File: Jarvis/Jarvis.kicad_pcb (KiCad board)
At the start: 2 copper layers, 30 x 50 mm, 137 parts, among them IC1 ADP1607, IC2 MAX-8Q, IC3 MPU-9250, IC4 STM32F411CxUx, IC5 Si4460, IC6 MS5611-01BA03, J1 PYRO, J2 PWR, J3 ARM, P1 SMA, P2 SMA, P3 SWD_TC, Q1 PFET, Q2 PFET, Q3 PFET, Q4 NFET, Q5 NFET, Q6 NFET, Q7 NFET, U1 MICROSD, Y1 26MHz, Y2 30MHz

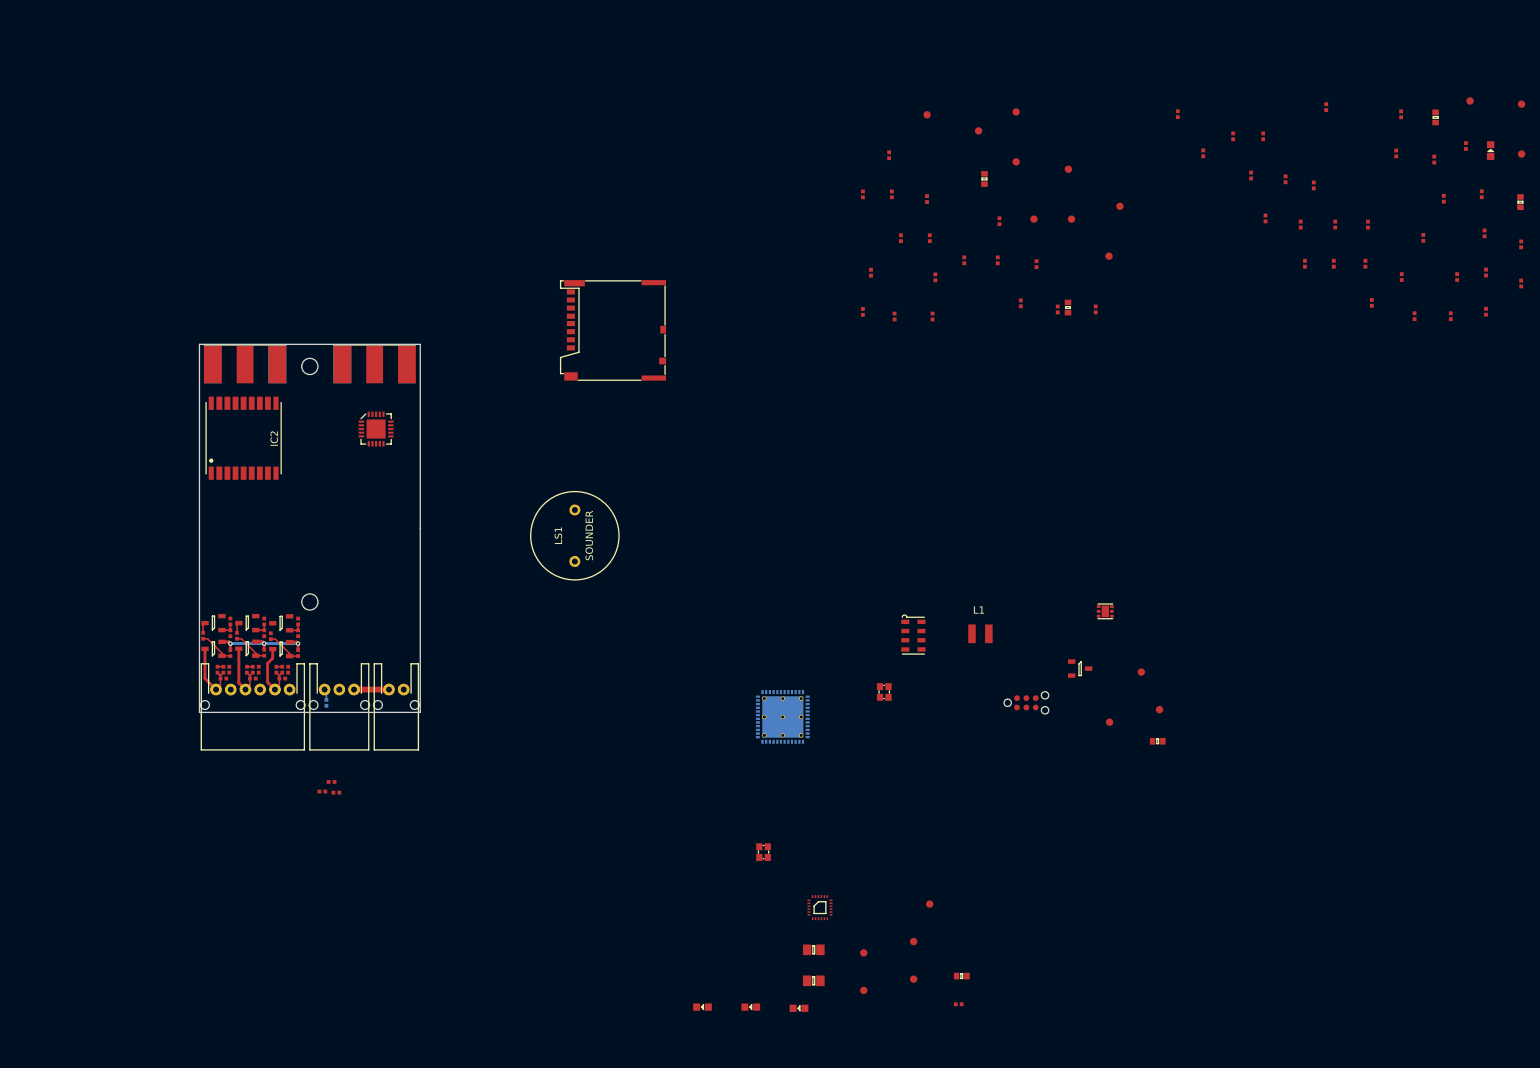
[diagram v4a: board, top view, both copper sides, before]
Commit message: Routed PSU
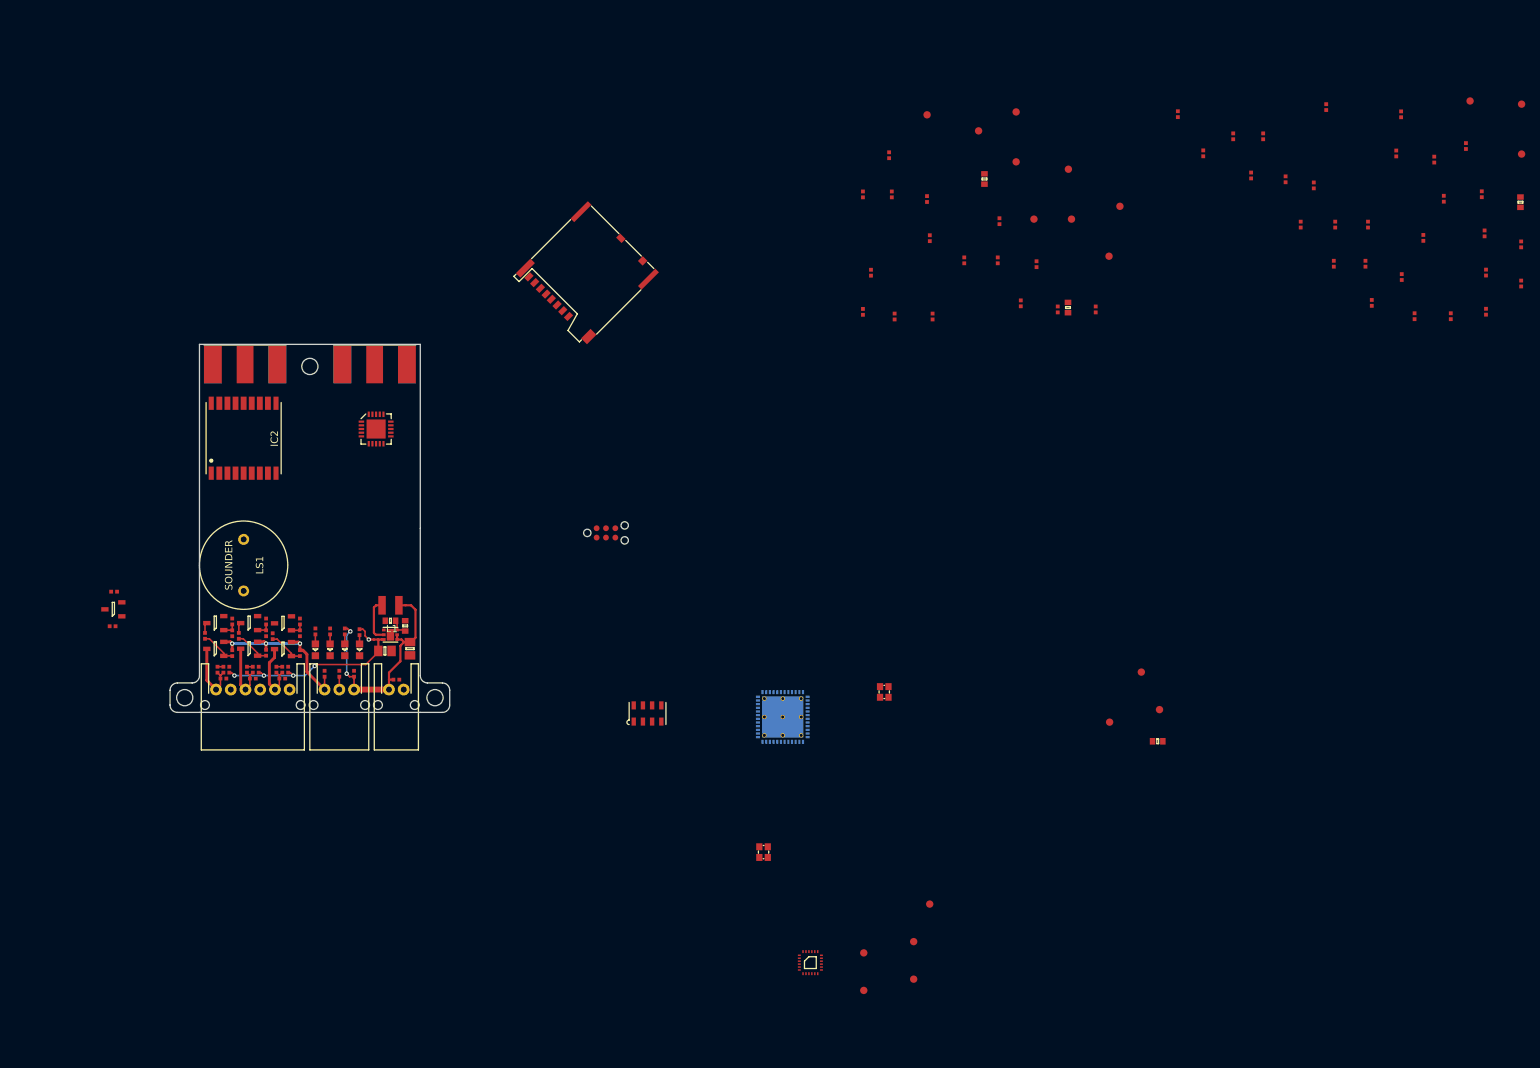
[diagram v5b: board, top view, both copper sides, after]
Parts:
- added REF**: MountingHole_2.2mm_M2_ISO14580, Mounting_Holes:MountingHole_2.2mm_M2_ISO14580, F.Cu at (117.0, 123.0)
- R25: moved to F.Cu
- moved D1 168.0 mm to (106.8, 116.5), turned to 90 degrees
- moved R34 167.8 mm to (73.4, 108.6), turned to 180 degrees
- moved R33 166.1 mm to (73.2, 113.3), turned to 0 degrees
- moved R23 160.5 mm to (102.8, 114.0)
- moved R7 156.1 mm to (113.0, 113.2), turned to 90 degrees
- moved Q7 131.6 mm to (73.3, 111.0), turned to 180 degrees
- moved R24 101.0 mm to (100.8, 114.0), turned to 270 degrees
- moved IC1 97.2 mm to (111.0, 114.5), turned to 180 degrees
- moved R22 92.5 mm to (104.8, 114.0)
- moved R21 91.9 mm to (106.8, 114.1)
- moved R11 91.4 mm to (111.0, 112.5), turned to 180 degrees
- moved L1 80.2 mm to (111.0, 110.5), turned to 180 degrees
- moved D2 78.6 mm to (104.8, 116.5), turned to 90 degrees
- moved D3 75.0 mm to (102.8, 116.5), turned to 90 degrees
- moved C3 73.5 mm to (110.2, 116.7)
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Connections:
- J3 pad 1: Net-(J3-Pad1) -> /PYRO_SO
- J3 pad 2: /PYRO_SO -> Net-(J3-Pad2)
- R25 pad 1: Net-(J3-Pad1) -> Net-(J3-Pad2)
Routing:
- net 3v3: track 0.00 -> 30.0 mm, vias 0 -> 5
- net VBATT: track 4.75 -> 33.1 mm, vias 0 -> 2
- net /PYRO_SO: track 15.8 -> 24.9 mm
- net Net-(IC1-Pad5): track 0.00 -> 6.13 mm
- net Net-(IC1-Pad3): track 0.00 -> 2.49 mm
- net Net-(J3-Pad2): track 0.00 -> 1.75 mm
- net Net-(J3-Pad1): track 1.50 -> 0.00 mm
- net Net-(D4-Pad2): track 0.00 -> 1.30 mm
- net Net-(D3-Pad2): track 0.00 -> 1.30 mm
- net Net-(D2-Pad2): track 0.00 -> 1.30 mm
- net Net-(D1-Pad2): track 0.00 -> 1.20 mm
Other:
- board size 30 x 50 mm -> 38 x 50 mm
- copper layers 2 -> 4
- net class Default: clearance 0.127 -> 0.15
- rule pad_to_mask_clearance: 0.2 -> 0
- rule trace_clearance: 0.127 -> 0.15

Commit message: Replaced SD Card with 16MB Flash and started placment
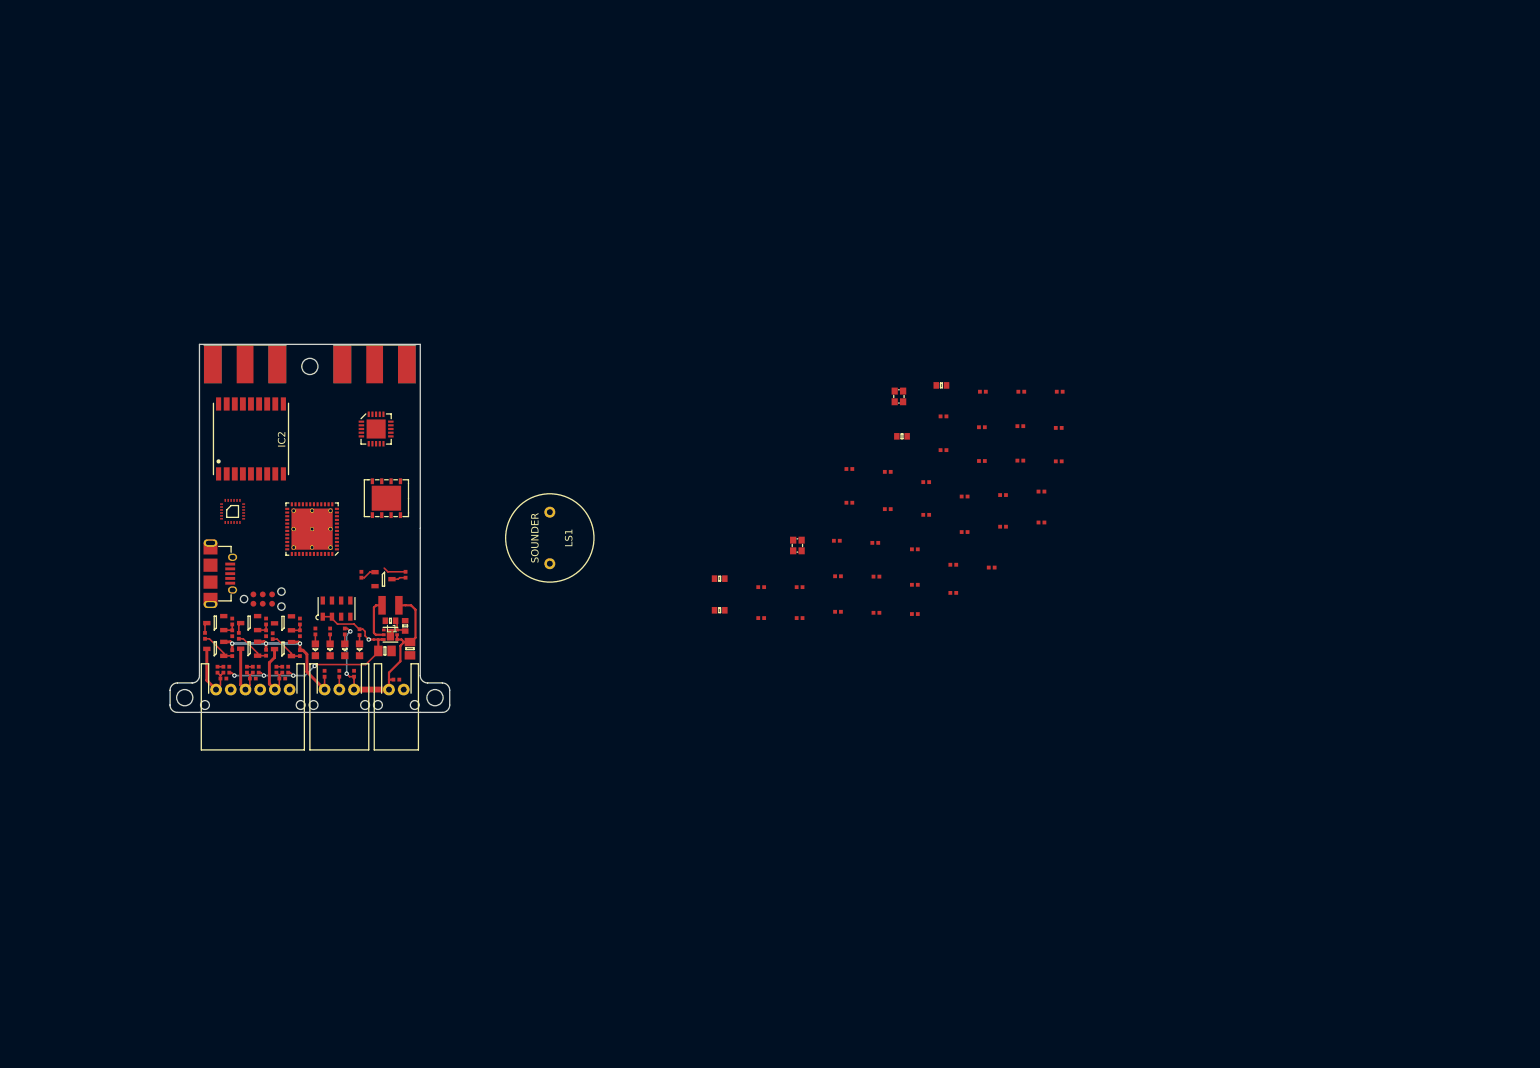
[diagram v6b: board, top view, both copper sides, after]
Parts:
- removed C29: 100nF, agg:0402-L
- removed R27, R28, R29, R30, R31: 47K, agg:0402-L
- removed TP1, TP10, TP11, TP12, TP13, TP14, TP15, TP16, TP17, TP18, TP19, TP2, TP20, TP3, TP4, TP5, TP6, TP7, TP8, TP9: TESTPAD, agg:TESTPAD
- removed U1: MICROSD, agg:MICROSD_MOLEX_503398-1892
- added IC7: S25FL127S, agg:WND008, F.Cu at (110.4, 95.9)
- added J4: MICROUSB, agg:MICROUSB_MOLEX_47589-0001, F.Cu at (86.5, 106.2)
- IC4: moved to F.Cu
- moved L7 122.1 mm to (155.7, 111.1), turned to 0 degrees
- moved C10 108.3 mm to (161.3, 108.0), turned to 0 degrees
- moved C14 107.0 mm to (166.5, 108.0), turned to 0 degrees
- moved IC3 99.6 mm to (89.5, 97.7)
- moved C34 95.0 mm to (177.0, 106.6), turned to 0 degrees
- moved C21 94.5 mm to (161.3, 112.2), turned to 0 degrees
- moved C30 92.4 mm to (171.8, 111.3), turned to 0 degrees
- moved FB2 91.9 mm to (177.0, 111.5), turned to 0 degrees
- moved C13 91.4 mm to (178.5, 92.3), turned to 0 degrees
- moved C22 91.3 mm to (166.5, 112.2), turned to 0 degrees
- moved C23 86.7 mm to (171.8, 106.5), turned to 0 degrees
- moved L6 85.1 mm to (187.4, 104.9), turned to 0 degrees
- moved C36 84.7 mm to (182.2, 102.8), turned to 0 degrees
- moved C35 81.0 mm to (189.0, 95.7), turned to 0 degrees
- moved R32 76.7 mm to (182.2, 111.6), turned to 0 degrees
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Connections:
- FB1 pad 1: /USART2_RX -> /USART1_RX
- FB2 pad 1: /USART2_TX -> /USART1_TX
- IC3 pad 22: /SPI5_NSS1 -> /SPI2_NSS1_MPU
- IC3 pad 23: /SPI5_SCK -> /SPI2_SCK
- IC3 pad 24: /SPI5_MOSI -> /SPI2_MOSI
- IC3 pad 9: /SPI5_MISO -> /SPI2_MISO
- IC4 pad 10: /BEEPER -> /PYRO1_S
- IC4 pad 11: /SPI4_MOSI -> /PYRO2_S
- IC4 pad 12: /USART2_TX -> /PYRO3_S
- IC4 pad 13: /USART2_RX -> /SPI1_NSS2_RADIO
- IC4 pad 14: /PYRO1_S -> /SPI1_NSS1_FLASH
- IC4 pad 15: /PYRO2_S -> /SPI1_SCK
- IC4 pad 16: /SDIO_CMD -> /SPI1_MISO
- IC4 pad 17: /PYRO3_S -> /SPI1_MOSI
- IC4 pad 18: /SPI5_SCK -> /Radio_nIRQ
- IC4 pad 19: /SPI5_NSS1 -> /GPS_RST
- IC4 pad 20: /GPS_RST -> Net-(IC4-Pad20)
- IC4 pad 21: /nIRQ -> /SPI2_SCK
- IC4 pad 25: /SPI4_NSS1 -> Net-(IC4-Pad25)
- IC4 pad 26: /SPI4_SCK -> /MPU_IRQ
- IC4 pad 27: /SD_CD -> /SPI2_MISO
- IC4 pad 28: /SDIO_CK -> /SPI2_MOSI
- IC4 pad 29: /SDIO_D1 -> Net-(IC4-Pad29)
- IC4 pad 30: /SDIO_D2 -> /USART1_TX
- IC4 pad 31: /SPI5_MOSI -> /USART1_RX
- IC4 pad 32: /SPI4_MISO -> /USB_OTG_DM
- IC4 pad 33: /SPI5_MISO -> /USB_OTG_DP
- IC4 pad 38: /MPU_IRQ -> Net-(IC4-Pad38)
- IC4 pad 4: Net-(IC4-Pad4) -> /BEEPER
- IC4 pad 40: /SDIO_D0 -> /PYRO2_F
- IC4 pad 41: /SDIO_D3 -> /PYRO3_F
- IC4 pad 42: /PYRO2_F -> /I2C1_SCL
- IC4 pad 43: /PYRO3_F -> /I2C1_SDA
- IC4 pad 45: /I2C1_SCL -> Net-(IC4-Pad45)
- IC4 pad 46: /I2C1_SDA -> /SPI2_NSS1_MPU
- IC5 pad 11: /nIRQ -> /Radio_nIRQ
- IC5 pad 12: /SPI4_SCK -> /SPI1_SCK
- IC5 pad 13: /SPI4_MISO -> /SPI1_MISO
- IC5 pad 14: /SPI4_MOSI -> /SPI1_MOSI
- IC5 pad 15: /SPI4_NSS1 -> /SPI1_NSS2_RADIO
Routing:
- net 3v3: track 30.0 -> 35.9 mm
- net Net-(LS1-Pad2): track 0.00 -> 3.11 mm
- net Net-(Q7-Pad1): track 0.00 -> 2.16 mm
- net Net-(Q7-Pad3): track 0.00 -> 1.93 mm

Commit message: Schematic Complete
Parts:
- added R27: 10k, agg:0402-L, F.Cu at (216.1, 63.9)
- added R28: 10k, agg:0402-L, F.Cu at (192.7, 87.2)
- added R29: 100R, agg:0402-L, F.Cu at (113.8, 101.2)
- added TP1: TESTPAD, agg:TESTPAD, F.Cu at (166.6, 90.9)
- added TP10: TESTPAD, agg:TESTPAD, F.Cu at (193.3, 73.4)
- added TP11: TESTPAD, agg:TESTPAD, F.Cu at (173.3, 93.4)
- added TP12: TESTPAD, agg:TESTPAD, F.Cu at (177.4, 68.4)
- added TP13: TESTPAD, agg:TESTPAD, F.Cu at (203.4, 63.4)
- added TP14: TESTPAD, agg:TESTPAD, F.Cu at (197.5, 68.4)
- added TP15: TESTPAD, agg:TESTPAD, F.Cu at (186.7, 78.4)
- added TP16: TESTPAD, agg:TESTPAD, F.Cu at (180.0, 83.4)
- added TP17: TESTPAD, agg:TESTPAD, F.Cu at (166.6, 95.9)
- added TP18: TESTPAD, agg:TESTPAD, F.Cu at (173.3, 88.4)
- added TP19: TESTPAD, agg:TESTPAD, F.Cu at (203.4, 58.4)
- added TP2: TESTPAD, agg:TESTPAD, F.Cu at (180.0, 93.4)
- added TP20: TESTPAD, agg:TESTPAD, F.Cu at (186.7, 73.4)
- added TP21: TESTPAD, agg:TESTPAD, F.Cu at (196.7, 63.4)
- added TP22: TESTPAD, agg:TESTPAD, F.Cu at (190.8, 68.4)
- added TP23: TESTPAD, agg:TESTPAD, F.Cu at (180.0, 78.4)
- added TP24: TESTPAD, agg:TESTPAD, F.Cu at (159.9, 77.8)
- added TP25: TESTPAD, agg:TESTPAD, F.Cu at (200.0, 73.4)
- added TP26: TESTPAD, agg:TESTPAD, F.Cu at (183.4, 63.4)
- added TP27: TESTPAD, agg:TESTPAD, F.Cu at (159.9, 97.8)
- added TP28: TESTPAD, agg:TESTPAD, F.Cu at (196.7, 58.4)
- added TP29: TESTPAD, agg:TESTPAD, F.Cu at (180.0, 73.4)
- added TP3: TESTPAD, agg:TESTPAD, F.Cu at (210.1, 63.4)
- added TP30: TESTPAD, agg:TESTPAD, F.Cu at (190.0, 63.4)
- added TP31: TESTPAD, agg:TESTPAD, F.Cu at (166.6, 85.9)
- added TP32: TESTPAD, agg:TESTPAD, F.Cu at (184.1, 68.4)
- added TP33: TESTPAD, agg:TESTPAD, F.Cu at (173.3, 78.4)
- added TP34: TESTPAD, agg:TESTPAD, F.Cu at (159.9, 92.8)
- added TP35: TESTPAD, agg:TESTPAD, F.Cu at (190.0, 58.4)
- added TP36: TESTPAD, agg:TESTPAD, F.Cu at (173.3, 73.4)
- added TP37: TESTPAD, agg:TESTPAD, F.Cu at (173.3, 83.4)
- added TP38: TESTPAD, agg:TESTPAD, F.Cu at (170.0, 58.4)
- added TP39: TESTPAD, agg:TESTPAD, F.Cu at (166.6, 80.9)
- added TP4: TESTPAD, agg:TESTPAD, F.Cu at (204.1, 68.4)
- added TP40: TESTPAD, agg:TESTPAD, F.Cu at (159.9, 87.8)
- added TP41: TESTPAD, agg:TESTPAD, F.Cu at (166.6, 75.9)
- added TP42: TESTPAD, agg:TESTPAD, F.Cu at (183.4, 58.4)
- added TP43: TESTPAD, agg:TESTPAD, F.Cu at (176.7, 63.4)
- added TP44: TESTPAD, agg:TESTPAD, F.Cu at (170.7, 68.4)
- added TP45: TESTPAD, agg:TESTPAD, F.Cu at (159.9, 82.8)
- added TP46: TESTPAD, agg:TESTPAD, F.Cu at (164.1, 70.9)
- added TP47: TESTPAD, agg:TESTPAD, F.Cu at (170.0, 63.4)
- added TP48: TESTPAD, agg:TESTPAD, F.Cu at (176.7, 58.4)
- added TP5: TESTPAD, agg:TESTPAD, F.Cu at (173.3, 98.4)
- added TP6: TESTPAD, agg:TESTPAD, F.Cu at (193.3, 78.4)
- added TP7: TESTPAD, agg:TESTPAD, F.Cu at (186.7, 83.4)
- added TP8: TESTPAD, agg:TESTPAD, F.Cu at (180.0, 88.4)
- added TP9: TESTPAD, agg:TESTPAD, F.Cu at (210.1, 58.4)
- LS1: footprint Library:ABI-042-RC -> Library:AI-1027-TWT-3V-R; moved to B.Cu
- moved C22 82.0 mm to (231.9, 62.6)
- moved Y1 75.9 mm to (106.4, 100.5), turned to 180 degrees
- moved C14 72.3 mm to (226.9, 68.3)
- moved L7 69.5 mm to (210.6, 68.5)
- moved C8 67.5 mm to (232.1, 71.9)
- moved C23 61.3 mm to (221.7, 70.9)
- moved C15 61.1 mm to (231.9, 58.4)
- moved C17 60.6 mm to (226.7, 63.2)
- moved C13 59.4 mm to (232.1, 66.8)
- moved C10 53.1 mm to (213.4, 97.6)
- moved C16 52.9 mm to (199.8, 77.6)
- moved C18 48.3 mm to (221.7, 75.7)
- moved C21 45.7 mm to (201.8, 91.0)
- moved C34 44.2 mm to (210.6, 78.0)
- moved C35 43.9 mm to (221.4, 66.1)
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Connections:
- IC4 pad 13: /SPI1_NSS2_RADIO -> /BATT_MON
- IC4 pad 29: Net-(IC4-Pad29) -> /SPI1_NSS2_RADIO
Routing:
- net Net-(Q7-Pad3): track 1.93 -> 3.51 mm
- net 3v3: track 35.9 -> 34.6 mm
- net Net-(Q7-Pad1): track 2.16 -> 1.35 mm
- net Net-(LS1-Pad2): track 3.11 -> 2.32 mm

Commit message: Routing progress
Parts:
- removed the REF** at (117.0, 123.0)
- moved L3 115.3 mm to (108.8, 85.9), turned to 90 degrees
- moved C23 112.8 mm to (110.0, 86.3), turned to 180 degrees
- moved L4 109.8 mm to (107.6, 83.8)
- moved C24 108.2 mm to (108.0, 85.9), turned to 90 degrees
- moved C28 106.8 mm to (107.6, 82.2), turned to 180 degrees
- moved L7 106.7 mm to (105.5, 86.9), turned to 180 degrees
- moved L2 103.8 mm to (108.4, 87.1)
- moved C25 102.1 mm to (107.2, 86.7), turned to 90 degrees
- moved L5 97.8 mm to (108.8, 83.4), turned to 90 degrees
- moved C27 94.0 mm to (110.0, 83.8)
- moved C26 91.0 mm to (106.4, 83.4), turned to 90 degrees
- moved R32 89.9 mm to (108.8, 81.8), turned to 90 degrees
- moved C30 87.7 mm to (103.8, 86.7), turned to 90 degrees
- moved L6 79.2 mm to (107.2, 85.1), turned to 90 degrees
- moved TP27 67.9 mm to (227.7, 103.1), turned to 90 degrees
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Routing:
- net 3v3: track 34.6 -> 14.2 mm, vias 5 -> 6
- net /I2C1_SDA: track 0.00 -> 5.15 mm
- net /I2C1_SCL: track 0.00 -> 3.90 mm
- net Net-(C24-Pad2): track 0.00 -> 3.87 mm
- net Net-(P2-Pad1): track 0.00 -> 3.65 mm
- net Net-(IC5-Pad16): track 0.00 -> 3.25 mm
- net Net-(C23-Pad2): track 0.00 -> 2.77 mm
- net Net-(C25-Pad1): track 0.00 -> 2.26 mm
- net Net-(C24-Pad1): track 0.00 -> 1.85 mm
- net Net-(IC5-Pad17): track 0.00 -> 1.72 mm
- net Net-(C28-Pad1): track 0.00 -> 1.60 mm
- net Net-(C27-Pad1): track 0.00 -> 1.60 mm
- net /~RST: track 0.00 -> 1.18 mm, vias 0 -> 1
- net Net-(C25-Pad2): track 0.00 -> 0.80 mm
- added copper zone on In2.Cu, net 3v3
- added copper zone on In1.Cu, net GND
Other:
- board size 38 x 50 mm -> 30 x 50 mm
